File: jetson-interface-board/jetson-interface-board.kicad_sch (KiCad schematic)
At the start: 22 parts, among them J1 Conn_01x04, J2 Conn_01x04, J3 USB_C_Receptacle_USB2.0, J4 Conn_01x06, J5 Conn_01x18, SW1 SW_Push, U1 MCP2562-E-MF, U2 FT234XD, U3 XC8111AA01MR-G, U4 XC8111AA01MR-G

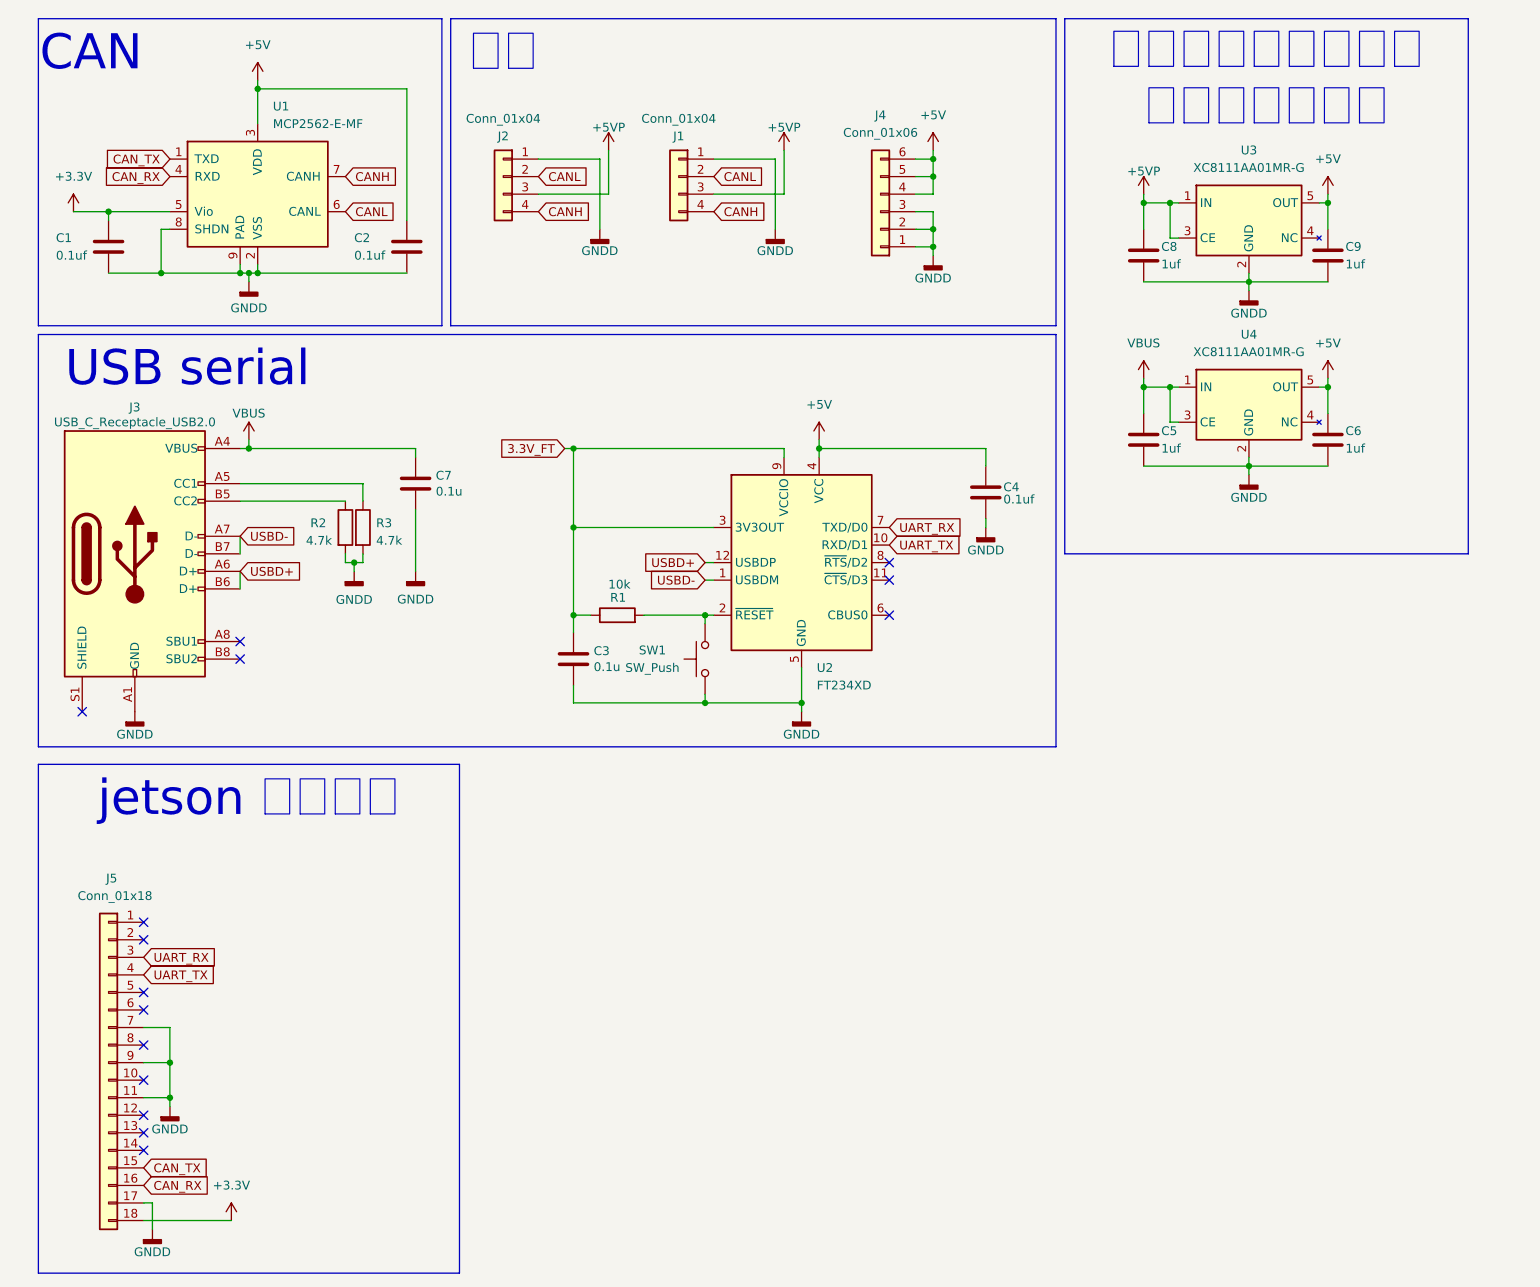
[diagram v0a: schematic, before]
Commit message: jetson-interface-board ビア以外完成
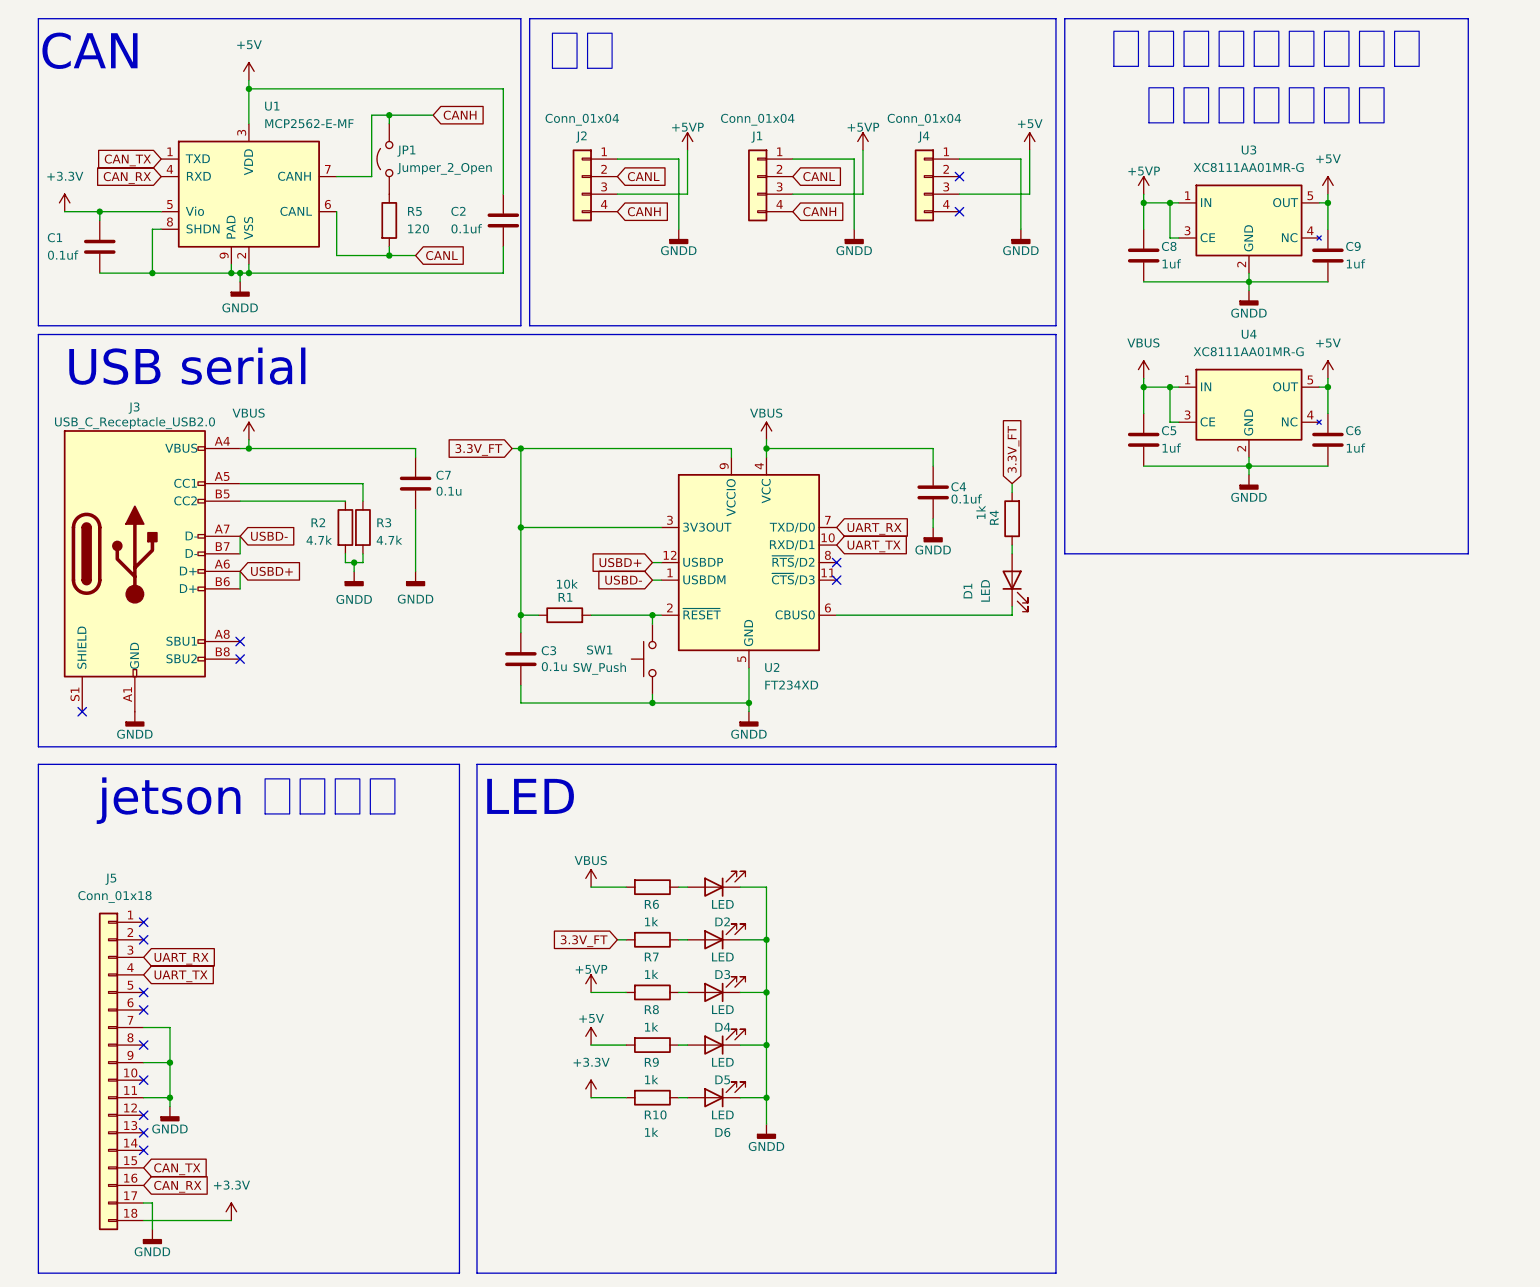
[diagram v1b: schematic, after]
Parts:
- removed J4: Conn_01x06, Connector_JST:JST_XH_B6B-XH-A_1x06_P2.50mm_Vertical, symbol Connector_Generic:Conn_01x06
- added D1, D2, D3, D4, D5, D6: LED, LED_SMD:LED_0603_1608Metric_Pad1.05x0.95mm_HandSolder, symbol Device:LED
- added J4: Conn_01x04, Connector_JST:JST_XH_B4B-XH-A_1x04_P2.50mm_Vertical, symbol Connector_Generic:Conn_01x04
- added JP1: Jumper_2_Open, Connector_PinHeader_2.54mm:PinHeader_1x02_P2.54mm_Vertical, symbol Jumper:Jumper_2_Open
- added R10, R4, R6, R7, R8, R9: 1k, Resistor_SMD:R_0603_1608Metric_Pad0.98x0.95mm_HandSolder, symbol Device:R
- added R5: 120, Resistor_SMD:R_0603_1608Metric_Pad0.98x0.95mm_HandSolder, symbol Device:R
- C1, C2: footprint (none) -> Capacitor_SMD:C_0603_1608Metric_Pad1.08x0.95mm_HandSolder
- J1, J2: footprint Connector_JST:JST_XH_B4B-XH-A_1x04_P2.50mm_Vertical -> Connector_JST:JST_XH_S4B-XH-A_1x04_P2.50mm_Horizontal
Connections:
- net +3.3V: now also R10.2
- net +5V: now also J4.3 (Pin_3), R9.2; no longer C4.1, U2.4 (VCC)
- net +5VP: now also R8.2
- net 3.3V_FT: now also R4.2, R7.2
- net CANH: now also JP1.2 (B)
- net CANL: now also R5.2
- net GNDD: now also D2.1 (K), D3.1 (K), D4.1 (K), D5.1 (K), D6.1 (K), J4.1 (Pin_1)
- net VBUS: now also C4.1, U2.4 (VCC), R6.2
- net at U2.6 (CBUS0): now also D1.1 (K)
- new net: D5.2 (A), R9.1
- new net: D3.2 (A), R7.1
- new net: JP1.1 (A), R5.1
- new net: D4.2 (A), R8.1
- new net: D2.2 (A), R6.1
- new net: D1.2 (A), R4.1
- new net: D6.2 (A), R10.1
- no-connect marks 15 -> 16
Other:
- note added: "LED"
- moved on the sheet: C1, C2, C3, C4, J1, J2, R1, SW1, U1, U2

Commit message: feat:インジケータとスイッチ変更および再配線・再配置
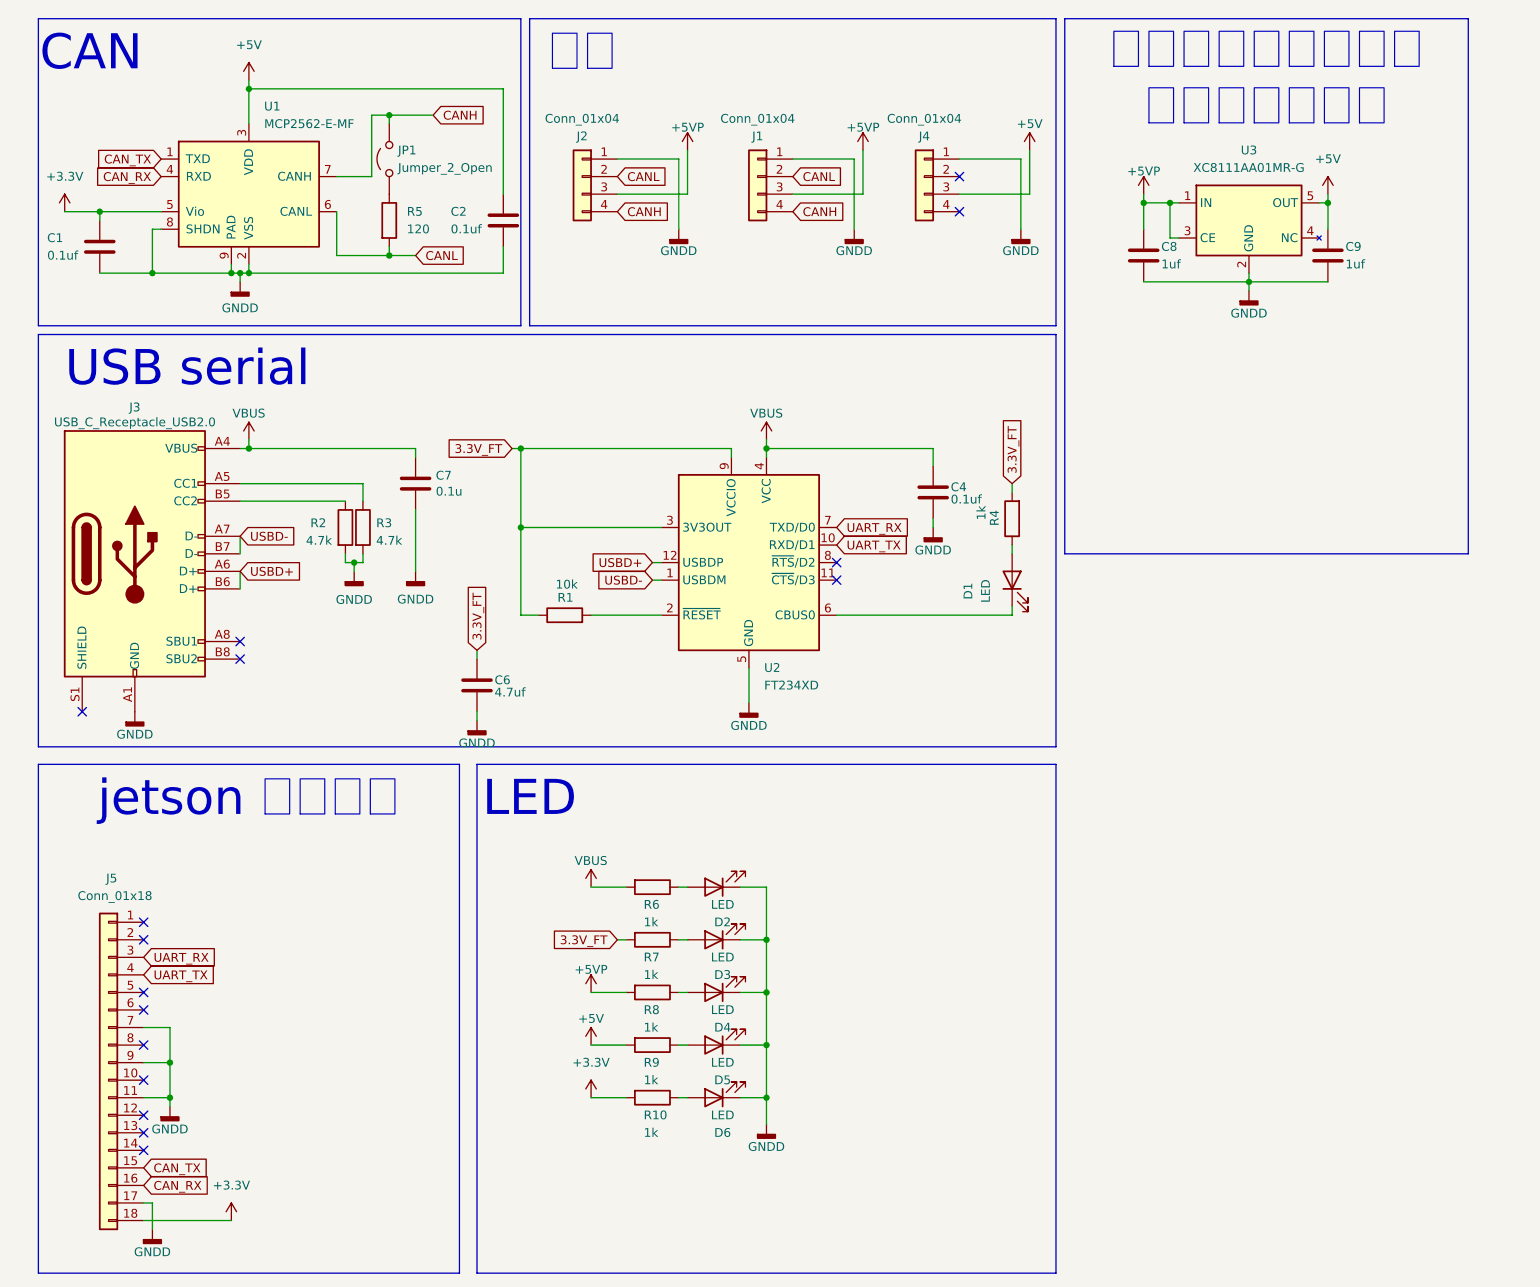
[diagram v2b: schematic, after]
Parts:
- removed C3: 0.1u, Capacitor_SMD:C_0603_1608Metric_Pad1.08x0.95mm_HandSolder, symbol Device:C
- removed C5: 1uf, Capacitor_SMD:C_0603_1608Metric_Pad1.08x0.95mm_HandSolder, symbol Device:C
- removed SW1: SW_Push, 0Ikedalibrary:switch_TVAF06-A020B-R, symbol Switch:SW_Push
- removed U4: XC8111AA01MR-G, Package_TO_SOT_SMD:SOT-23-5, symbol Power_Management:AP22913CN4
- C6: value 1uf -> 4.7uf
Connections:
- net +5V: no longer C6.1
- net 3.3V_FT: now also C6.1

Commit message: fix:[WIP]pin header
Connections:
- net +3.3V: now also J5.15 (Pin_15); no longer J5.18 (Pin_18)
- net CAN_RX: now also J5.17 (Pin_17); no longer J5.16 (Pin_16)
- net CAN_TX: now also J5.18 (Pin_18); no longer J5.15 (Pin_15)
- net GNDD: now also J5.16 (Pin_16), J5.2 (Pin_2), J5.4 (Pin_4), J5.6 (Pin_6); no longer J5.11 (Pin_11), J5.17 (Pin_17), J5.7 (Pin_7), J5.9 (Pin_9)
- net UART_RX: now also J5.10 (Pin_10); no longer J5.3 (Pin_3)
- net UART_TX: now also J5.9 (Pin_9); no longer J5.4 (Pin_4)
